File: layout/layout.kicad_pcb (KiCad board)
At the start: 4 copper layers, 11.1 x 45 mm, 32 parts, among them J1 ?, J2 SJ-3523-SMT-TR, Q1 MMBT3904, Q2 MMBT3906, Q3 MMBT3906

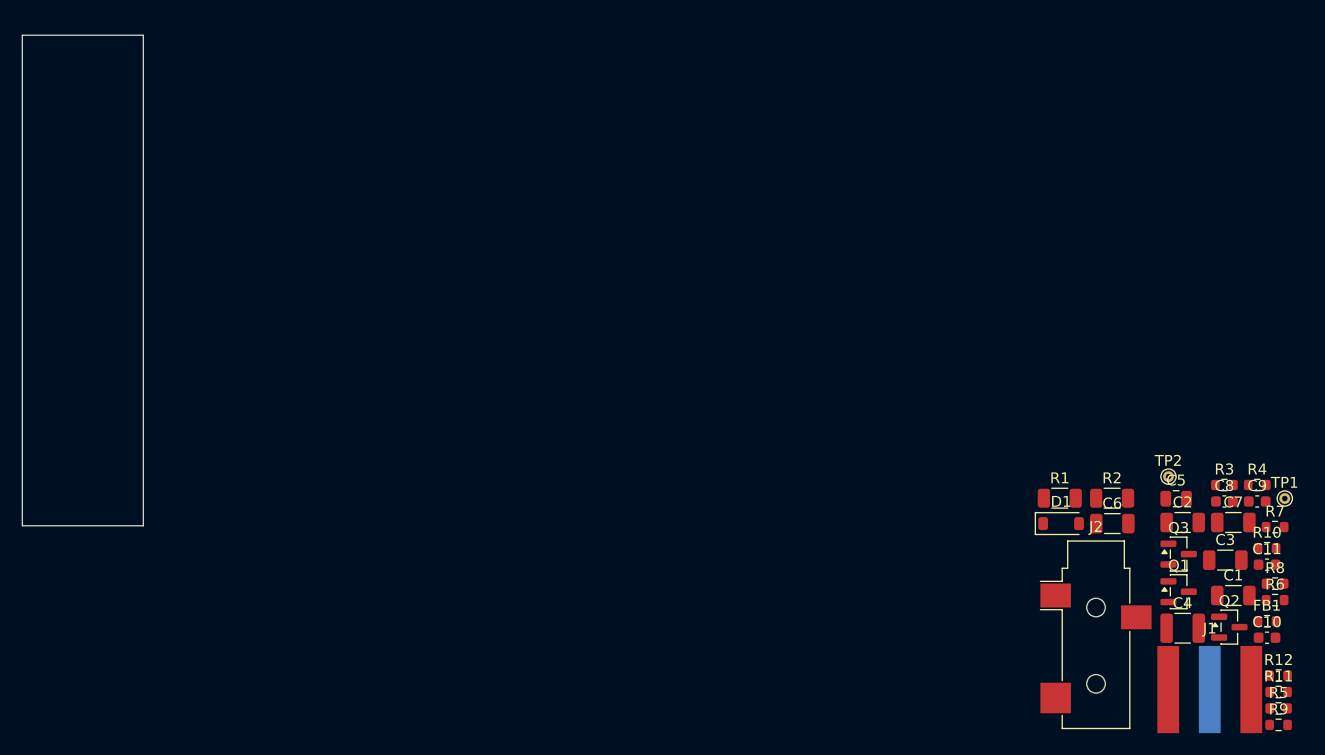
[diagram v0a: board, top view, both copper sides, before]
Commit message: Layout: rigenerato per J1 a filo, spessore 1.6mm standard, outline provvisorio 30x40mm (guscio esterno)
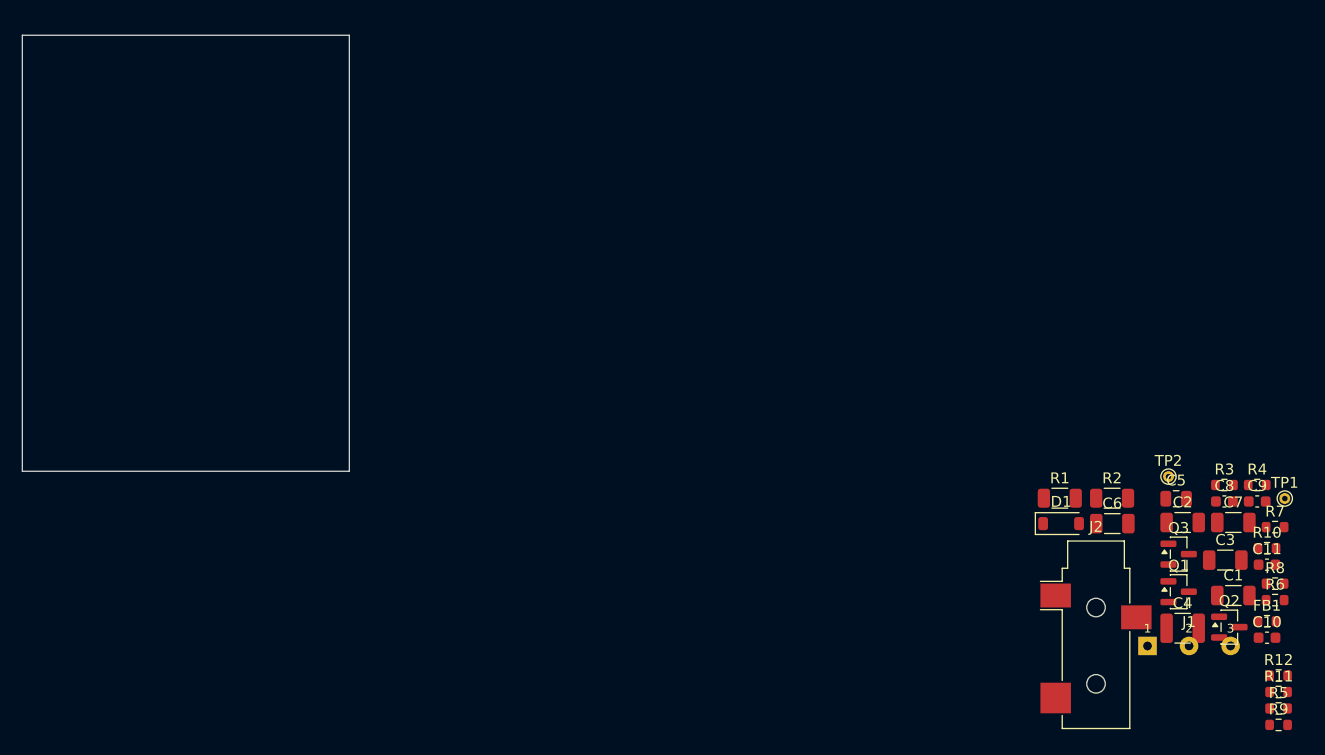
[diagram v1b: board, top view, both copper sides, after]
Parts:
- J1: footprint iu3qez_electret2xlr_footprints:J1_NC3MXX_Sandwich -> iu3qez_electret2xlr_footprints:J1_XLR3_WirePads
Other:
- board size 11.1 x 45 mm -> 30 x 40 mm
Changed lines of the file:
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@@
 	(generator_version "10.0")
 	(general
-		(thickness 0.8)
+		(thickness 1.6062)
 		(legacy_teardrops no)
 	)
@@
 	(layer "dielectric 2"
 		(type "core")
-		(thickness 0.26)
+		(thickness 1.065)
 		(material "FR4-Core")
 		(epsilon_r 4.6)
@@
 		)
 	)
-	(footprint "iu3qez_electret2xlr_footprints:J1_NC3MXX_Sandwich"
-		(layer "F.Cu")
-		(at 153.225 106.025)
-		(descr "Custom sandwich mount for Neutrik NC3MXX 3-pin male XLR chassis connector. Solder-cup pitch 7.62mm. Three 8mm-long pads (2mm wide) at board XLR edge: pin1 (GND) FRONT x=1.90mm, pin2 (P2) FRONT x=9.52mm, pin3 (P3) BACK x=5.71mm. Origin = board XLR edge / left corner, pads extend from y=0 (edge) to y=8mm.")
-		(tags "XLR NC3MXX sandwich phantom")
-		(property "Reference" "J1"
-			(at 5.71 -1.6 0)
-			(layer "F.SilkS")
-			(effects
-				(font
-					(size 1 1)
-					(thickness 0.15)
-				)
-			)
-		)
-		(property "Value" "?"
-			(at 5.71 9.6 0)
-			(layer "F.Fab")
-			(hide yes)
-			(effects
-				(font
-					(size 1 1)
-					(thickness 0.15)
-				)
-			)
-		)
-		(property "Datasheet" ""
-			(at 0 0 0)
-			(layer "F.Fab")
-			(hide yes)
-			(effects
-				(font
-					(size 1.27 1.27)
-					(thickness 0.15)
-				)
-			)
-		)
-		(property "Description" "XLR Connector, Male or Female, 3 Pins"
-			(at 0 0 0)
-			(layer "F.Fab")
-			(hide yes)
-			(effects
-				(font
-					(size 1.27 1.27)
-					(thickness 0.15)
-				)
-			)
-		)
-		(property "Path" "J1"
-			(at 0 0 0)
-			(layer "F.SilkS")
-			(hide yes)
-			(effects
-				(font
-					(size 1.27 1.27)
-					(thickness 0.15)
-				)
-			)
-		)
-		(property "Prefix" "J"
-			(at 0 0 0)
-			(layer "F.SilkS")
-			(hide yes)
-			(effects
-				(font
-					(size 1.27 1.27)
-					(thickness 0.15)
-				)
-			)
-		)
-		(attr smd exclude_from_bom)
-		(duplicate_pad_numbers_are_jumpers no)
-		(fp_line
-			(start 0.6 0)
-			(end 0.6 8)
-			(stroke
-				(width 0.1)
-				(type solid)
-			)
-			(layer "F.Fab")
-		)
-		(fp_line
-			(start 10.82 0)
-			(end 10.82 8)
-			(stroke
-				(width 0.1)
-				(type solid)
-			)
-			(layer "F.Fab")
-		)
-		(fp_text user "${REFERENCE}"
-			(at 5.71 4 0)
-			(layer "F.Fab")
-			(effects
-				(font
-					(size 1 1)
-					(thickness 0.15)
-				)
-			)
-		)
-		(pad "1" smd rect
-			(at 1.9 4)
-			(size 2 8)
-			(layers "F.Cu" "F.Mask" "F.Paste")
-			(net "GND")
-		)
-		(pad "2" smd rect
-			(at 9.52 4)
-			(size 2 8)
-			(layers "F.Cu" "F.Mask" "F.Paste")
-			(net "P2")
-		)
-		(pad "3" smd rect
-			(at 5.71 4)
-			(size 2 8)
-			(layers "B.Cu" "B.Mask" "B.Paste")
-			(net "P3")
-		)
-		(embedded_fonts no)
-	)
 	(footprint "stdlib_kicad-footprints_Capacitor_SMD:C_0805_2012Metric"
 		(layer "F.Cu")
@@
 		)
 	)
+	(footprint "iu3qez_electret2xlr_footprints:J1_XLR3_WirePads"
+		(layer "F.Cu")
+		(at 153.225 106.025)
+		(descr "Tre piazzole THT per saldare i fili del cavetto verso uno spinotto XLR maschio volante (NC3MX). pin1=GND/schermo, pin2=hot, pin3=cold. Passo 3.81mm, foro 0.8mm per filo fino a ~0.5mm. Sostituisce il montaggio sandwich in-connettore.")
+		(tags "XLR wire pads flying-lead")
+		(property "Reference" "J1"
+			(at 3.81 -2.2 0)
+			(layer "F.SilkS")
+			(effects
+				(font
+					(size 1 1)
+					(thickness 0.15)
+				)
+			)
+		)
+		(property "Value" "?"
+			(at 3.81 2.4 0)
+			(layer "F.Fab")
+			(hide yes)
+			(effects
+				(font
+					(size 1 1)
+					(thickness 0.15)
+				)
+			)
+		)
+		(property "Datasheet" ""
+			(at 0 0 0)
+			(layer "F.Fab")
+			(hide yes)
+			(effects
+				(font
+					(size 1.27 1.27)
+					(thickness 0.15)
+				)
+			)
+		)
+		(property "Description" "XLR Connector, Male or Female, 3 Pins"
+			(at 0 0 0)
+			(layer "F.Fab")
+			(hide yes)
+			(effects
+				(font
+					(size 1.27 1.27)
+					(thickness 0.15)
+				)
+			)
+		)
+		(property "Path" "J1"
+			(at 0 0 0)
+			(layer "F.SilkS")
+			(hide yes)
+			(effects
+				(font
+					(size 1.27 1.27)
+				)
+			)
+		)
+		(property "Prefix" "J"
+			(at 0 0 0)
+			(layer "F.SilkS")
+			(hide yes)
+			(effects
+				(font
+					(size 1.27 1.27)
+				)
+			)
+		)
+		(attr through_hole exclude_from_bom)
+		(duplicate_pad_numbers_are_jumpers no)
+		(fp_text user "1"
+			(at 0 -1.6 0)
+			(layer "F.SilkS")
+			(effects
+				(font
+					(size 0.8 0.8)
+					(thickness 0.12)
+				)
+			)
+		)
+		(fp_text user "2"
+			(at 3.81 -1.6 0)
+			(layer "F.SilkS")
+			(effects
+				(font
+					(size 0.8 0.8)
+					(thickness 0.12)
+				)
+			)
+		)
+		(fp_text user "3"
+			(at 7.62 -1.6 0)
+			(layer "F.SilkS")
+			(effects
+				(font
+					(size 0.8 0.8)
+					(thickness 0.12)
+				)
+			)
+		)
+		(pad "1" thru_hole rect
+			(at 0 0)
+			(size 1.7 1.7)
+			(drill 0.8)
+			(layers "*.Cu" "*.Mask")
+			(remove_unused_layers no)
+			(net "GND")
+		)
+		(pad "2" thru_hole circle
+			(at 3.81 0)
+			(size 1.7 1.7)
+			(drill 0.8)
+			(layers "*.Cu" "*.Mask")
+			(remove_unused_layers no)
+			(net "P2")
+		)
+		(pad "3" thru_hole circle
+			(at 7.62 0)
+			(size 1.7 1.7)
+			(drill 0.8)
+			(layers "*.Cu" "*.Mask")
+			(remove_unused_layers no)
+			(net "P3")
+		)
+		(embedded_fonts no)
+	)
 	(footprint "stdlib_kicad-footprints_Resistor_SMD:R_0603_1608Metric"
 		(layer "F.Cu")
@@
 	(gr_rect
 		(start 50.0 50.0)
-		(end 61.1 95.0)
+		(end 80.0 90.0)
 		(stroke (width 0.1) (type default))
 		(fill none)

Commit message: Layout: outline board 50x40mm e placement iniziale dei componenti dentro il bordo
30x40 provvisorio troppo stretto per 32 componenti + piani di massa; parti spostate dentro l'outline con prime tracce.
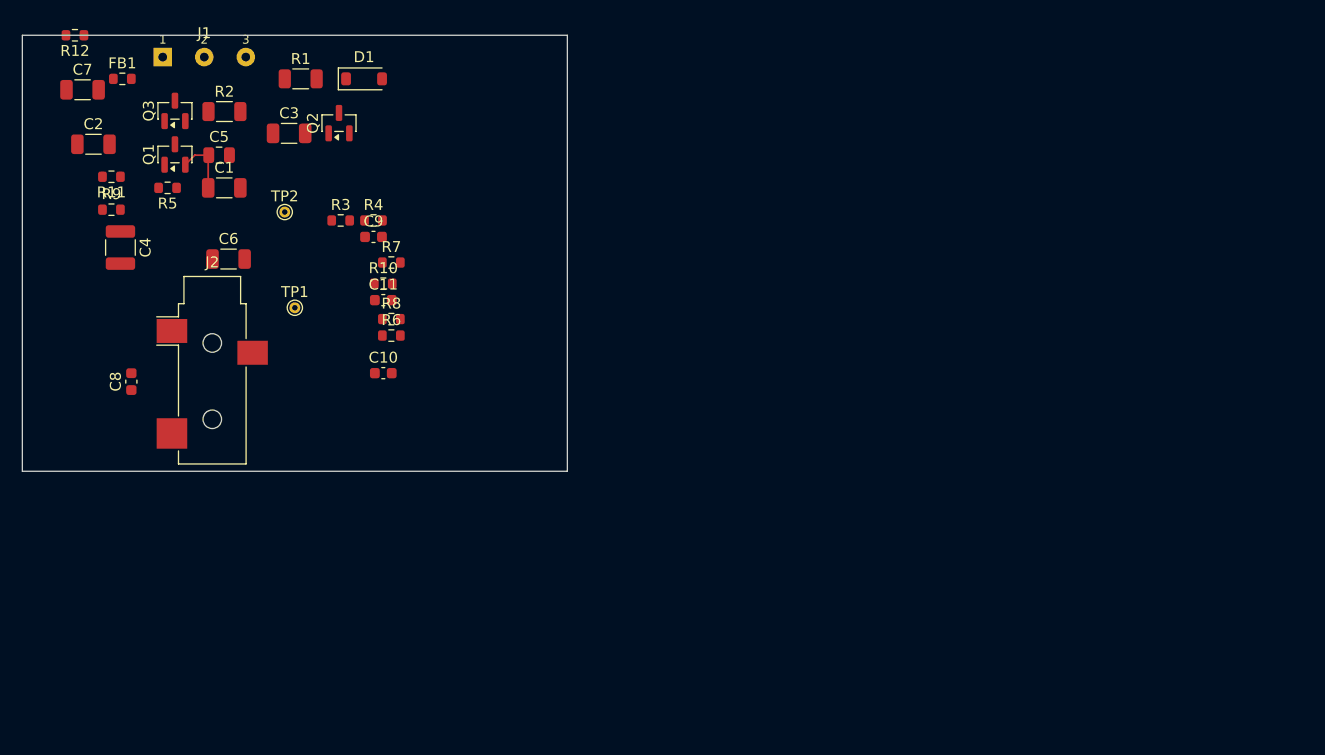
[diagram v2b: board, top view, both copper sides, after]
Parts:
- moved R12 125.1 mm to (54.8, 50.0), turned to 180 degrees
- moved R11 117.0 mm to (58.2, 63.0), turned to 180 degrees
- moved R9 117.0 mm to (58.2, 66.0)
- moved FB1 116.2 mm to (59.2, 54.0)
- moved C7 112.8 mm to (55.5, 55.0)
- moved R5 112.6 mm to (63.3, 64.0), turned to 180 degrees
- moved C2 105.8 mm to (56.5, 60.0)
- moved J1 105.3 mm to (62.9, 52.0)
- moved C4 103.5 mm to (59.0, 69.5), turned to -90 degrees
- moved C8 100.9 mm to (60.0, 81.8), turned to 90 degrees
- moved Q3 100.7 mm to (64.0, 56.9), turned to 90 degrees
- moved Q1 100.4 mm to (64.0, 60.9), turned to 90 degrees
- moved C1 99.8 mm to (68.5, 64.0)
- moved C3 94.4 mm to (74.5, 59.0)
- moved Q2 93.9 mm to (79.0, 58.1), turned to 90 degrees
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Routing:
- net VPIP: track 0.00 -> 5.53 mm
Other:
- board size 30 x 40 mm -> 50 x 40 mm
